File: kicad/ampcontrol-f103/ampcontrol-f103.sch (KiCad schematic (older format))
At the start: 69 parts, among them J1 SP, J10 Buttons, J11 Encoder, J12 LCD_CTRL, J13 I2C, J14 I2C, J15 I2C, J16 SPI_2.4, J17 SPI_2.8, J18 SPI_3.2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

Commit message: Kicad: Fix arduino-specific pinout
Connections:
- net +3V3: now also J20.4 (Pin_4); no longer J20.3 (Pin_3)
- net +5V: now also J20.5 (Pin_5); no longer J20.4 (Pin_4)
- net SCL: now also J22.1 (Pin_1); no longer J22.2 (Pin_2)
- net SDA: now also J22.2 (Pin_2); no longer J22.3 (Pin_3)
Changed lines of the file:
@@
 EESchema Schematic File Version 4
 LIBS:ampcontrol-f103-cache
-EELAYER 26 0
+EELAYER 29 0
 EELAYER END
 $Descr A4 11693 8268
@@
 NoConn ~ 10750 2700
 NoConn ~ 10750 2800
-NoConn ~ 10750 3100
+NoConn ~ 10750 2900
 NoConn ~ 10750 3400
 $Comp
 L power:+3V3 #PWR048
 U 1 1 5CAA18DB
-P 10600 2800
-F 0 "#PWR048" H 10600 2650 50  0001 C CNN
-F 1 "+3V3" H 10615 2973 50  0000 C CNN
-F 2 "" H 10600 2800 50  0001 C CNN
-F 3 "" H 10600 2800 50  0001 C CNN
-	1    10600 2800
-	1    0    0    -1
-$EndComp
-Wire Wire Line
-	10750 2900 10600 2900
-Wire Wire Line
-	10600 2900 10600 2800
+P 10600 2750
+F 0 "#PWR048" H 10600 2600 50  0001 C CNN
+F 1 "+3V3" H 10615 2923 50  0000 C CNN
+F 2 "" H 10600 2750 50  0001 C CNN
+F 3 "" H 10600 2750 50  0001 C CNN
+	1    10600 2750
+	1    0    0    -1
+$EndComp
+Wire Wire Line
+	10750 3000 10600 3000
+Wire Wire Line
+	10600 3000 10600 2750
 $Comp
 L power:+5V #PWR046
 U 1 1 5CABB371
-P 10350 2800
-F 0 "#PWR046" H 10350 2650 50  0001 C CNN
-F 1 "+5V" H 10365 2973 50  0000 C CNN
-F 2 "" H 10350 2800 50  0001 C CNN
-F 3 "" H 10350 2800 50  0001 C CNN
-	1    10350 2800
-	1    0    0    -1
-$EndComp
-Wire Wire Line
-	10350 2800 10350 3000
-Wire Wire Line
-	10350 3000 10750 3000
+P 10350 2750
+F 0 "#PWR046" H 10350 2600 50  0001 C CNN
+F 1 "+5V" H 10365 2923 50  0000 C CNN
+F 2 "" H 10350 2750 50  0001 C CNN
+F 3 "" H 10350 2750 50  0001 C CNN
+	1    10350 2750
+	1    0    0    -1
+$EndComp
+Wire Wire Line
+	10350 2750 10350 3100
+Wire Wire Line
+	10350 3100 10750 3100
 $Comp
 L power:GNDD #PWR047
@@
 RX1
 Wire Wire Line
+	10750 5400 10450 5400
+Wire Wire Line
 	10750 5500 10450 5500
-Wire Wire Line
-	10750 5600 10450 5600
-NoConn ~ 10750 5400
+NoConn ~ 10750 5600
+Text Label 10450 5400 0    50   ~ 0
+SCL
 Text Label 10450 5500 0    50   ~ 0
-SCL
-Text Label 10450 5600 0    50   ~ 0
 SDA
 Wire Wire Line

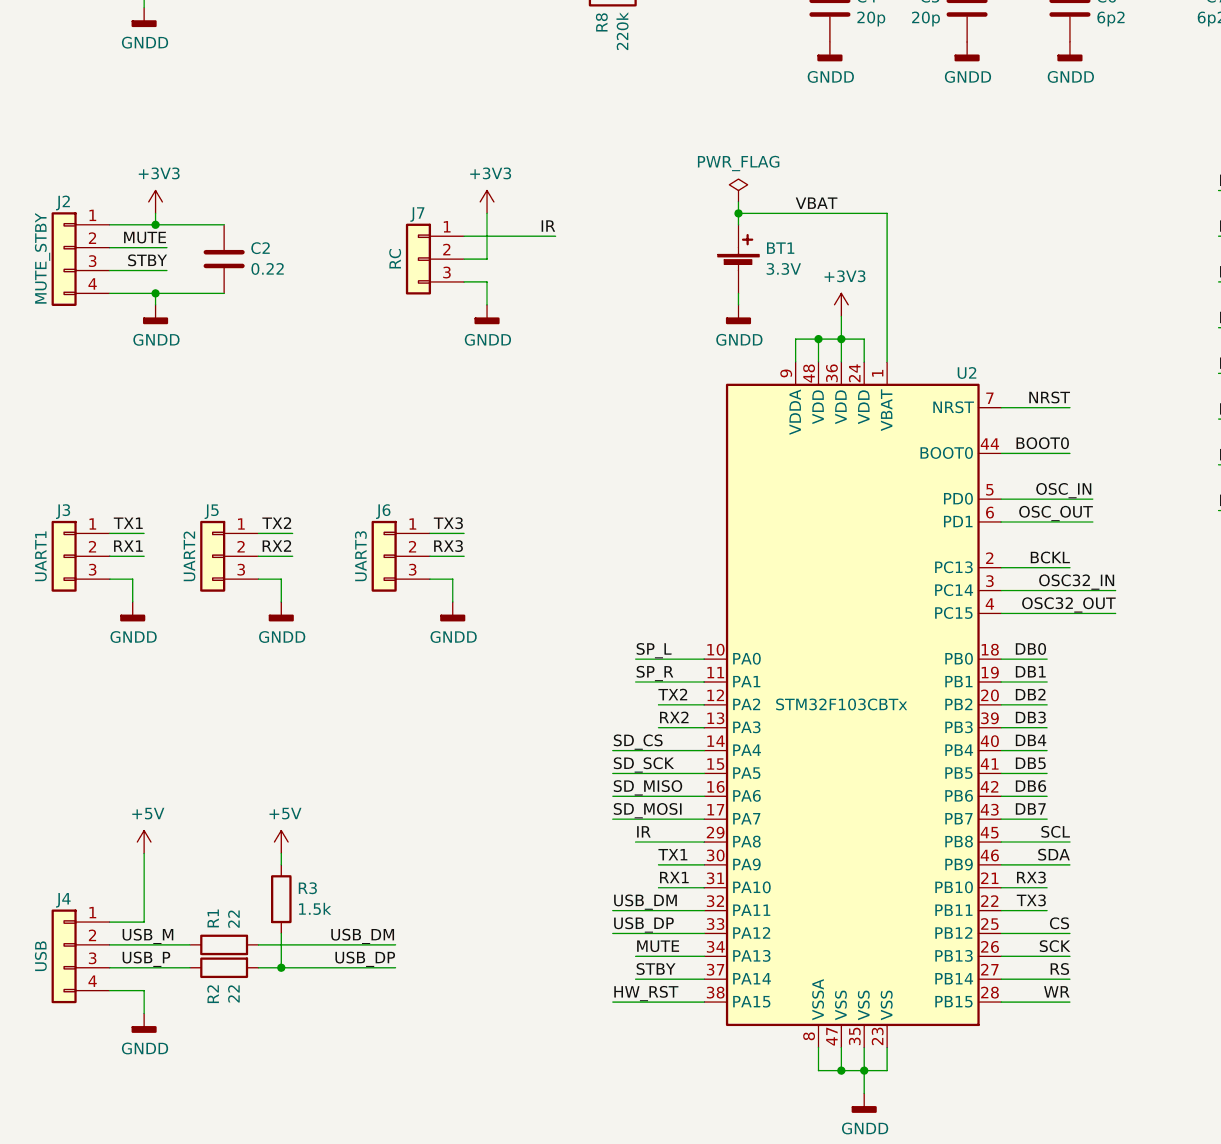
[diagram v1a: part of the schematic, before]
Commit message: Schematic: map MUTE/STBY to PB11/PB10, that are de-facto have been used
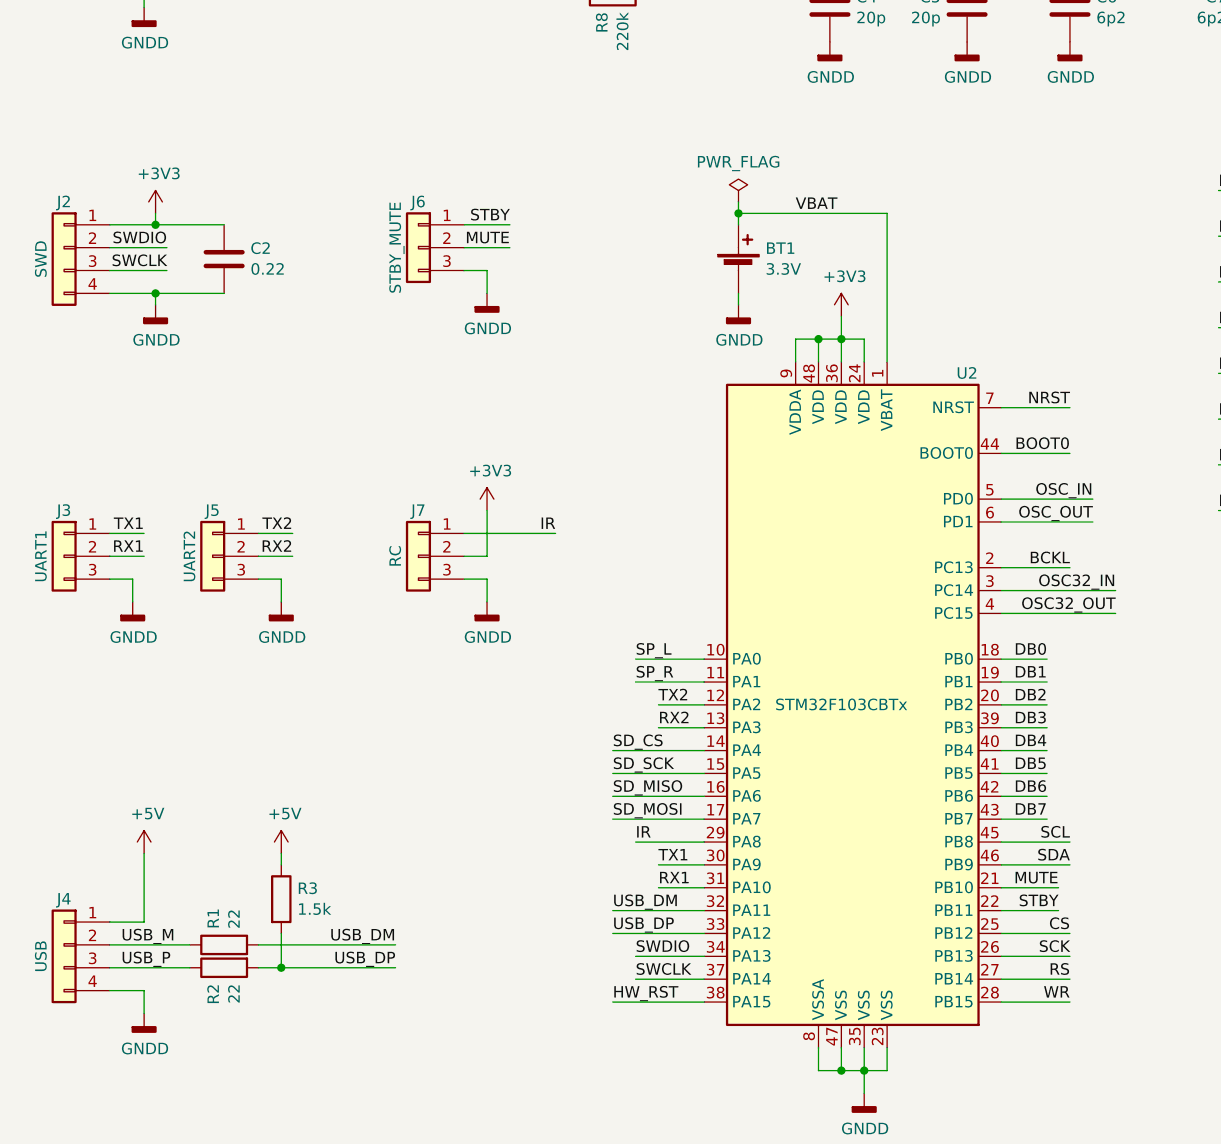
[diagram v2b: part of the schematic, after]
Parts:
- J2: value MUTE_STBY -> SWD
- J6: value UART3 -> STBY_MUTE
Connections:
- net RX3 is gone; now on net MUTE: J6.2 (Pin_2), U2.21 (PB10)
- net TX3 is gone; now on net STBY: J6.1 (Pin_1), U2.22 (PB11)
- net MUTE: no longer J2.2 (Pin_2), U2.34 (PA13)
- net STBY: no longer J2.3 (Pin_3), U2.37 (PA14)
- new net SWCLK: J2.3 (Pin_3), U2.37 (PA14)
- new net SWDIO: J2.2 (Pin_2), U2.34 (PA13)
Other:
- moved on the sheet: J6, J7
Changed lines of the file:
@@
 EESchema Schematic File Version 4
-LIBS:ampcontrol-f103-cache
-EELAYER 29 0
+EELAYER 30 0
 EELAYER END
 $Descr A4 11693 8268
@@
 Wire Wire Line
 	3250 7000 3550 7000
-Text Label 3250 6900 0    50   ~ 0
-MUTE
-Text Label 3250 7000 0    50   ~ 0
-STBY
 Wire Wire Line
 	3550 6400 3250 6400
@@
 SDA
 Wire Wire Line
-	4850 6600 5050 6600
-Wire Wire Line
-	4850 6700 5050 6700
-Text Label 5050 6600 2    50   ~ 0
-RX3
-Text Label 5050 6700 2    50   ~ 0
-TX3
-Wire Wire Line
 	8700 5350 8700 5450
 Wire Wire Line
@@
 	3450 1400 3650 1400
 $Comp
-L Connector_Generic:Conn_01x03 J7
-U 1 1 5DD7E4BF
-P 2300 3850
-F 0 "J7" H 2300 4050 50  0000 C CNN
-F 1 "RC" V 2400 3850 50  0000 C CNN
-F 2 "Connector_PinHeader_2.54mm:PinHeader_1x03_P2.54mm_Vertical" H 2300 3850 50  0001 C CNN
-F 3 "~" H 2300 3850 50  0001 C CNN
-	1    2300 3850
-	-1   0    0    -1
-$EndComp
-$Comp
-L power:+3V3 #PWR016
-U 1 1 5DD7E66F
-P 2600 3650
-F 0 "#PWR016" H 2600 3500 50  0001 C CNN
-F 1 "+3V3" H 2615 3823 50  0000 C CNN
-F 2 "" H 2600 3650 50  0001 C CNN
-F 3 "" H 2600 3650 50  0001 C CNN
-	1    2600 3650
-	1    0    0    -1
-$EndComp
-Wire Wire Line
-	2600 3650 2600 3850
-Wire Wire Line
-	2600 3850 2500 3850
-$Comp
-L power:GNDD #PWR017
-U 1 1 5DD9A47F
-P 2600 4050
-F 0 "#PWR017" H 2600 3800 50  0001 C CNN
-F 1 "GNDD" H 2604 3895 50  0000 C CNN
-F 2 "" H 2600 4050 50  0001 C CNN
-F 3 "" H 2600 4050 50  0001 C CNN
-	1    2600 4050
-	1    0    0    -1
-$EndComp
-Wire Wire Line
-	2600 4050 2600 3950
-Wire Wire Line
-	2600 3950 2500 3950
-Wire Wire Line
-	2500 3750 2900 3750
-Text Label 2900 3750 2    50   ~ 0
-IR
-$Comp
 L power:PWR_FLAG #FLG01
 U 1 1 5DE0D5C5
@@
 Wire Wire Line
 	1450 4000 1150 4000
-Text Label 1200 3800 2    50   ~ 0
-MUTE
 Wire Wire Line
 	950  3800 1200 3800
-Text Label 1200 3900 2    50   ~ 0
-STBY
 Wire Wire Line
 	950  3900 1200 3900
-$Comp
-L Connector_Generic:Conn_01x04 J2
-U 1 1 5D6B946E
-P 750 3800
-F 0 "J2" H 750 4000 50  0000 C CNN
-F 1 "MUTE_STBY" V 850 3750 50  0000 C CNN
-F 2 "Connector_PinHeader_2.54mm:PinHeader_1x04_P2.54mm_Vertical" H 750 3800 50  0001 C CNN
-F 3 "~" H 750 3800 50  0001 C CNN
-	1    750  3800
-	-1   0    0    -1
-$EndComp
 Wire Wire Line
 	950  6850 1300 6850
@@
 Text Label 1750 5050 2    50   ~ 0
 TX2
-Wire Wire Line
-	2350 5150 2500 5150
-Text Label 2500 5150 2    50   ~ 0
-RX3
-Wire Wire Line
-	2350 5050 2500 5050
-Text Label 2500 5050 2    50   ~ 0
-TX3
 $Comp
 L power:+5V #PWR043
@@
 $EndComp
 $Comp
-L Connector_Generic:Conn_01x03 J6
-U 1 1 5C758977
-P 2150 5150
-F 0 "J6" H 2150 5350 50  0000 C CNN
-F 1 "UART3" V 2250 5150 50  0000 C CNN
-F 2 "Connector_PinHeader_2.54mm:PinHeader_1x03_P2.54mm_Vertical" H 2150 5150 50  0001 C CNN
-F 3 "~" H 2150 5150 50  0001 C CNN
-	1    2150 5150
-	-1   0    0    -1
-$EndComp
-$Comp
 L power:GNDD #PWR06
 U 1 1 5C758F61
@@
 	1    0    0    -1
 $EndComp
-$Comp
-L power:GNDD #PWR013
-U 1 1 5C7E0BB5
-P 2450 5350
-F 0 "#PWR013" H 2450 5100 50  0001 C CNN
-F 1 "GNDD" H 2454 5195 50  0000 C CNN
-F 2 "" H 2450 5350 50  0001 C CNN
-F 3 "" H 2450 5350 50  0001 C CNN
-	1    2450 5350
-	1    0    0    -1
-$EndComp
 Wire Wire Line
 	950  5250 1050 5250
@@
 Wire Wire Line
 	1700 5250 1700 5350
-Wire Wire Line
-	2350 5250 2450 5250
-Wire Wire Line
-	2450 5250 2450 5350
 Wire Wire Line
 	9750 1700 9750 2200
@@
 Wire Wire Line
 	10300 5700 10300 5750
+$Comp
+L Connector_Generic:Conn_01x04 J2
+U 1 1 5D6B946E
+P 750 3800
+F 0 "J2" H 750 4000 50  0000 C CNN
+F 1 "SWD" V 850 3750 50  0000 C CNN
+F 2 "Connector_PinHeader_2.54mm:PinHeader_1x04_P2.54mm_Vertical" H 750 3800 50  0001 C CNN
+F 3 "~" H 750 3800 50  0001 C CNN
+	1    750  3800
+	-1   0    0    -1
+$EndComp
+Text Label 3250 6900 0    50   ~ 0
+SWDIO
+Text Label 3250 7000 0    50   ~ 0
+SWCLK
+Text Label 1200 3800 2    50   ~ 0
+SWDIO
+Text Label 1200 3900 2    50   ~ 0
+SWCLK
+$Comp
+L Connector_Generic:Conn_01x03 J7
+U 1 1 5DD7E4BF
+P 2300 5150
+F 0 "J7" H 2300 5350 50  0000 C CNN
+F 1 "RC" V 2400 5150 50  0000 C CNN
+F 2 "Connector_PinHeader_2.54mm:PinHeader_1x03_P2.54mm_Vertical" H 2300 5150 50  0001 C CNN
+F 3 "~" H 2300 5150 50  0001 C CNN
+	1    2300 5150
+	-1   0    0    -1
+$EndComp
+$Comp
+L power:+3V3 #PWR016
+U 1 1 5DD7E66F
+P 2600 4950
+F 0 "#PWR016" H 2600 4800 50  0001 C CNN
+F 1 "+3V3" H 2615 5123 50  0000 C CNN
+F 2 "" H 2600 4950 50  0001 C CNN
+F 3 "" H 2600 4950 50  0001 C CNN
+	1    2600 4950
+	1    0    0    -1
+$EndComp
+Wire Wire Line
+	2600 4950 2600 5150
+Wire Wire Line
+	2600 5150 2500 5150
+$Comp
+L power:GNDD #PWR017
+U 1 1 5DD9A47F
+P 2600 5350
+F 0 "#PWR017" H 2600 5100 50  0001 C CNN
+F 1 "GNDD" H 2604 5195 50  0000 C CNN
+F 2 "" H 2600 5350 50  0001 C CNN
+F 3 "" H 2600 5350 50  0001 C CNN
+	1    2600 5350
+	1    0    0    -1
+$EndComp
+Wire Wire Line
+	2600 5350 2600 5250
+Wire Wire Line
+	2600 5250 2500 5250
+Wire Wire Line
+	2500 5050 2900 5050
+Text Label 2900 5050 2    50   ~ 0
+IR
+Wire Wire Line
+	2500 3800 2700 3800
+Text Label 2700 3800 2    50   ~ 0
+MUTE
+Wire Wire Line
+	2500 3700 2700 3700
+Text Label 2700 3700 2    50   ~ 0
+STBY
+$Comp
+L Connector_Generic:Conn_01x03 J6
+U 1 1 5C758977
+P 2300 3800
+F 0 "J6" H 2300 4000 50  0000 C CNN
+F 1 "STBY_MUTE" V 2400 3800 50  0000 C CNN
+F 2 "Connector_PinHeader_2.54mm:PinHeader_1x03_P2.54mm_Vertical" H 2300 3800 50  0001 C CNN
+F 3 "~" H 2300 3800 50  0001 C CNN
+	1    2300 3800
+	-1   0    0    -1
+$EndComp
+$Comp
+L power:GNDD #PWR013
+U 1 1 5C7E0BB5
+P 2600 4000
+F 0 "#PWR013" H 2600 3750 50  0001 C CNN
+F 1 "GNDD" H 2604 3845 50  0000 C CNN
+F 2 "" H 2600 4000 50  0001 C CNN
+F 3 "" H 2600 4000 50  0001 C CNN
+	1    2600 4000
+	1    0    0    -1
+$EndComp
+Wire Wire Line
+	2500 3900 2600 3900
+Wire Wire Line
+	2600 3900 2600 4000
+Wire Wire Line
+	4850 6600 5100 6600
+Wire Wire Line
+	4850 6700 5100 6700
+Text Label 5100 6600 2    50   ~ 0
+MUTE
+Text Label 5100 6700 2    50   ~ 0
+STBY
 $EndSCHEMATC

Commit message: Small changes in schematic/PCB
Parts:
- added R24, R25: 0, Resistor_SMD:R_0805_2012Metric, symbol Device:R
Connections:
- net HW_RST: now also R25.1
- net NRST: now also R24.1; no longer J12.4 (Pin_4), J19.5 (Pin_5)
- new net RST: J12.4 (Pin_4), J19.5 (Pin_5), R24.2, R25.2
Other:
- note added: "R24: installed\nR25: not installed"
- moved on the sheet: J19
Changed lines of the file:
@@
 Text Label 8600 3350 0    50   ~ 0
 CS
-Text Label 8900 5450 0    50   ~ 0
+Text Label 9200 5450 0    50   ~ 0
 NRST
 Text Label 8600 3850 0    50   ~ 0
@@
 	8700 5950 8700 6050
 Wire Wire Line
-	8700 5450 9100 5450
+	8700 5450 9550 5450
 Text Label 9350 2100 0    50   ~ 0
 SDA
@@
 	8600 3450 8850 3450
 Text Label 8600 3450 0    50   ~ 0
-NRST
+RST
 Wire Wire Line
 	4550 1450 4550 1500
@@
 L Connector_Generic:Conn_01x06 J19
 U 1 1 5C9416D3
-P 10950 2150
-F 0 "J19" H 10950 2450 50  0000 C CNN
-F 1 "Arduino_Analog" V 11050 2100 50  0000 C CNN
-F 2 "Connector_PinSocket_2.54mm:PinSocket_1x06_P2.54mm_Vertical" H 10950 2150 50  0001 C CNN
-F 3 "~" H 10950 2150 50  0001 C CNN
-	1    10950 2150
+P 10950 1700
+F 0 "J19" H 10950 2000 50  0000 C CNN
+F 1 "Arduino_Analog" V 11050 1650 50  0000 C CNN
+F 2 "Connector_PinSocket_2.54mm:PinSocket_1x06_P2.54mm_Vertical" H 10950 1700 50  0001 C CNN
+F 3 "~" H 10950 1700 50  0001 C CNN
+	1    10950 1700
 	1    0    0    -1
 $EndComp
@@
 $EndComp
 Wire Wire Line
-	10750 1950 10500 1950
-Text Label 10500 1950 0    50   ~ 0
+	10750 1500 10500 1500
+Text Label 10500 1500 0    50   ~ 0
 RD
 Wire Wire Line
-	10750 2050 10500 2050
-Text Label 10500 2050 0    50   ~ 0
+	10750 1600 10500 1600
+Text Label 10500 1600 0    50   ~ 0
 WR
 Wire Wire Line
-	10750 2150 10500 2150
-Text Label 10500 2150 0    50   ~ 0
+	10750 1700 10500 1700
+Text Label 10500 1700 0    50   ~ 0
 RS
 Wire Wire Line
-	10500 2250 10750 2250
-Text Label 10500 2250 0    50   ~ 0
+	10500 1800 10750 1800
+Text Label 10500 1800 0    50   ~ 0
 CS
 Wire Wire Line
-	10750 2350 10500 2350
-Text Label 10500 2350 0    50   ~ 0
-NRST
-Wire Wire Line
-	10750 2450 10500 2450
-Text Label 10500 2450 0    50   ~ 0
+	10750 1900 10500 1900
+Text Label 10500 1900 0    50   ~ 0
+RST
+Wire Wire Line
+	10750 2000 10500 2000
+Text Label 10500 2000 0    50   ~ 0
 BCKL
 NoConn ~ 10750 2700
 NoConn ~ 10750 2800
-NoConn ~ 10750 2900
 NoConn ~ 10750 3400
-$Comp
-L power:+3V3 #PWR048
-U 1 1 5CAA18DB
-P 10600 2750
-F 0 "#PWR048" H 10600 2600 50  0001 C CNN
-F 1 "+3V3" H 10615 2923 50  0000 C CNN
-F 2 "" H 10600 2750 50  0001 C CNN
-F 3 "" H 10600 2750 50  0001 C CNN
-	1    10600 2750
-	1    0    0    -1
-$EndComp
-Wire Wire Line
-	10750 3000 10600 3000
-Wire Wire Line
-	10600 3000 10600 2750
 $Comp
 L power:+5V #PWR046
@@
 Text Label 5100 6700 2    50   ~ 0
 STBY
+$Comp
+L Device:R R24
+U 1 1 5E3B5B38
+P 9700 5450
+F 0 "R24" H 9750 5500 50  0000 L CNN
+F 1 "0" H 9750 5400 50  0000 L CNN
+F 2 "Resistor_SMD:R_0805_2012Metric" V 9630 5450 50  0001 C CNN
+F 3 "~" H 9700 5450 50  0001 C CNN
+	1    9700 5450
+	0    -1   -1   0
+$EndComp
+Wire Wire Line
+	9850 5450 10050 5450
+Text Label 10050 5450 2    50   ~ 0
+RST
+Wire Wire Line
+	10750 3000 10600 3000
+Wire Wire Line
+	10600 3000 10600 2750
+$Comp
+L power:+3V3 #PWR048
+U 1 1 5CAA18DB
+P 10600 2750
+F 0 "#PWR048" H 10600 2600 50  0001 C CNN
+F 1 "+3V3" H 10615 2923 50  0000 C CNN
+F 2 "" H 10600 2750 50  0001 C CNN
+F 3 "" H 10600 2750 50  0001 C CNN
+	1    10600 2750
+	1    0    0    -1
+$EndComp
+NoConn ~ 10750 2900
+$Comp
+L Device:R R25
+U 1 1 5E4BA951
+P 9700 5800
+F 0 "R25" H 9750 5850 50  0000 L CNN
+F 1 "0" H 9750 5750 50  0000 L CNN
+F 2 "Resistor_SMD:R_0805_2012Metric" V 9630 5800 50  0001 C CNN
+F 3 "~" H 9700 5800 50  0001 C CNN
+	1    9700 5800
+	0    -1   -1   0
+$EndComp
+Wire Wire Line
+	9850 5800 10050 5800
+Text Label 10050 5800 2    50   ~ 0
+RST
+Wire Wire Line
+	9550 5800 9200 5800
+Text Label 9200 5800 0    50   ~ 0
+HW_RST
+Text Notes 9350 6100 0    50   ~ 0
+R24: installed\nR25: not installed
 $EndSCHEMATC
